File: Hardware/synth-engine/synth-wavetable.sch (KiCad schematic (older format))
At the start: 0 parts

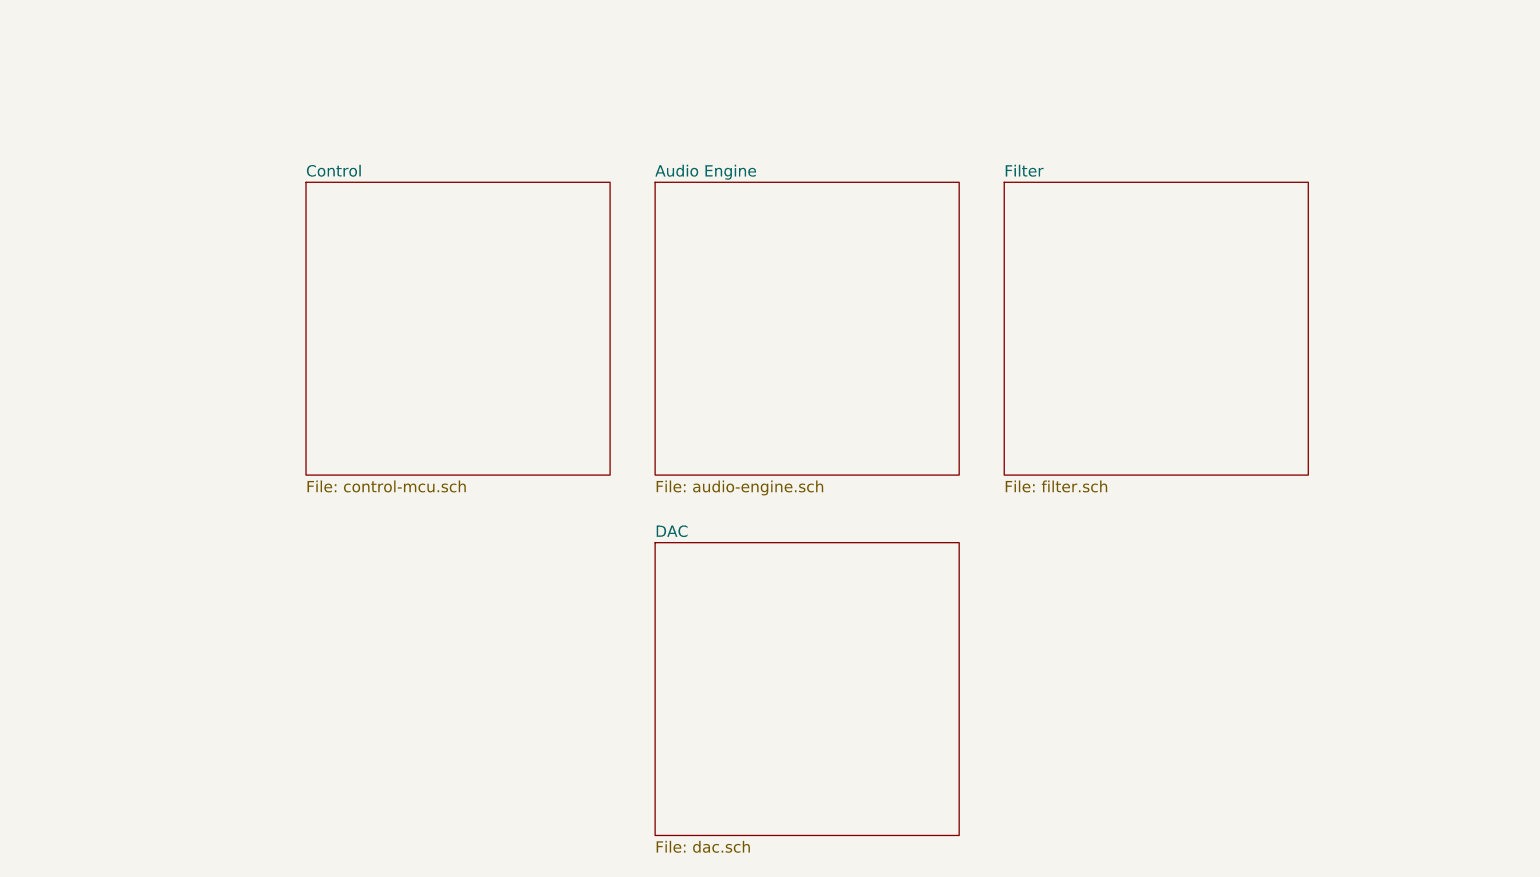
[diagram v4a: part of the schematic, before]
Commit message: add I/O connections between DAC and STM32 pages
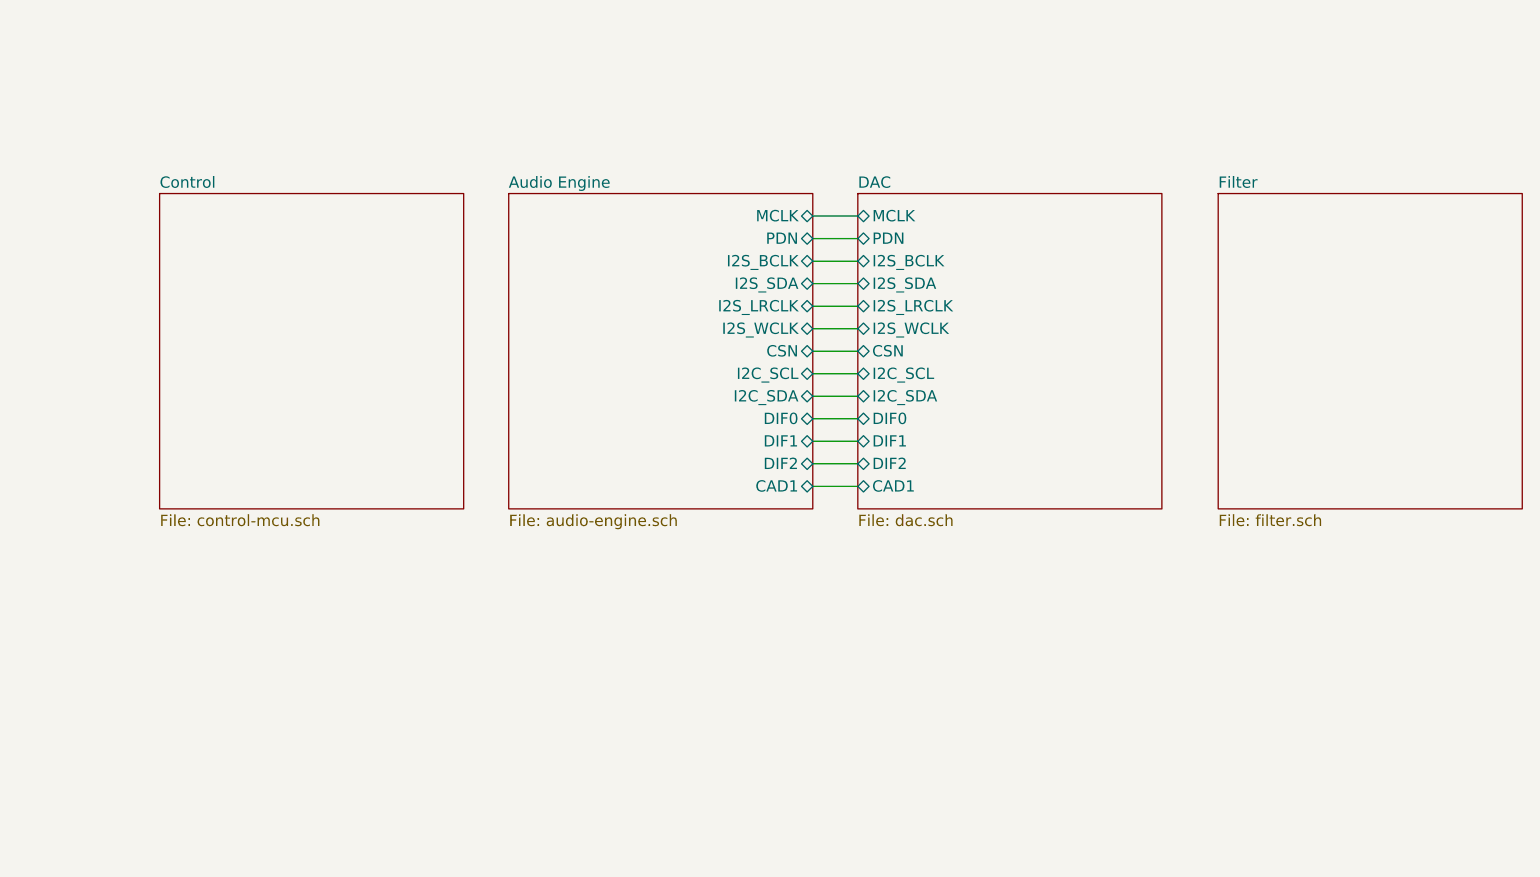
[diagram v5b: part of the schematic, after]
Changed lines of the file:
@@
 $EndDescr
 $Sheet
-S 3500 3450 1350 1300
+S 2850 3500 1350 1400
 U 5DDBDEEA
 F0 "Control" 50
@@
 $EndSheet
 $Sheet
-S 5050 3450 1350 1300
+S 4400 3500 1350 1400
 U 5DDC7BB6
 F0 "Audio Engine" 50
 F1 "audio-engine.sch" 50
+F2 "PDN" B R 5750 3700 50
+F3 "I2S_BCLK" B R 5750 3800 50
+F4 "I2S_SDA" B R 5750 3900 50
+F5 "I2S_LRCLK" B R 5750 4000 50
+F6 "I2S_WCLK" B R 5750 4100 50
+F7 "CSN" B R 5750 4200 50
+F8 "I2C_SCL" B R 5750 4300 50
+F9 "I2C_SDA" B R 5750 4400 50
+F10 "DIF0" B R 5750 4500 50
+F11 "DIF1" B R 5750 4600 50
+F12 "DIF2" B R 5750 4700 50
+F13 "MCLK" B R 5750 3600 50
+F14 "CAD1" B R 5750 4800 50
 $EndSheet
 $Sheet
-S 6600 3450 1350 1300
+S 7550 3500 1350 1400
 U 5DDC7E61
 F0 "Filter" 50
@@
 $EndSheet
 $Sheet
-S 5050 5050 1350 1300
+S 5950 3500 1350 1400
 U 5DD9C8DD
 F0 "DAC" 50
 F1 "dac.sch" 50
+F2 "MCLK" B L 5950 3600 50
+F3 "PDN" B L 5950 3700 50
+F4 "I2S_BCLK" B L 5950 3800 50
+F5 "I2S_SDA" B L 5950 3900 50
+F6 "I2S_LRCLK" B L 5950 4000 50
+F7 "I2S_WCLK" B L 5950 4100 50
+F8 "CSN" B L 5950 4200 50
+F9 "I2C_SCL" B L 5950 4300 50
+F10 "I2C_SDA" B L 5950 4400 50
+F11 "DIF0" B L 5950 4500 50
+F12 "DIF1" B L 5950 4600 50
+F13 "DIF2" B L 5950 4700 50
+F14 "CAD1" B L 5950 4800 50
 $EndSheet
+Wire Wire Line
+	5750 3600 5950 3600
+Wire Wire Line
+	5950 3700 5750 3700
+Wire Wire Line
+	5750 3800 5950 3800
+Wire Wire Line
+	5950 3900 5750 3900
+Wire Wire Line
+	5750 4000 5950 4000
+Wire Wire Line
+	5950 4100 5750 4100
+Wire Wire Line
+	5750 4200 5950 4200
+Wire Wire Line
+	5950 4300 5750 4300
+Wire Wire Line
+	5750 4400 5950 4400
+Wire Wire Line
+	5950 4500 5750 4500
+Wire Wire Line
+	5750 4600 5950 4600
+Wire Wire Line
+	5950 4700 5750 4700
+Wire Wire Line
+	5750 4800 5950 4800
 $EndSCHEMATC

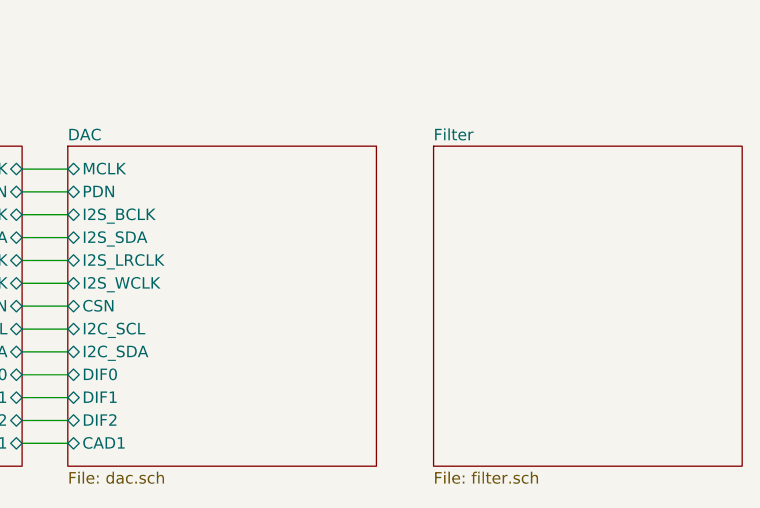
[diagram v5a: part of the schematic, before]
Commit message: add LFP following DAC diff outputs and connect DAC output to VCF input
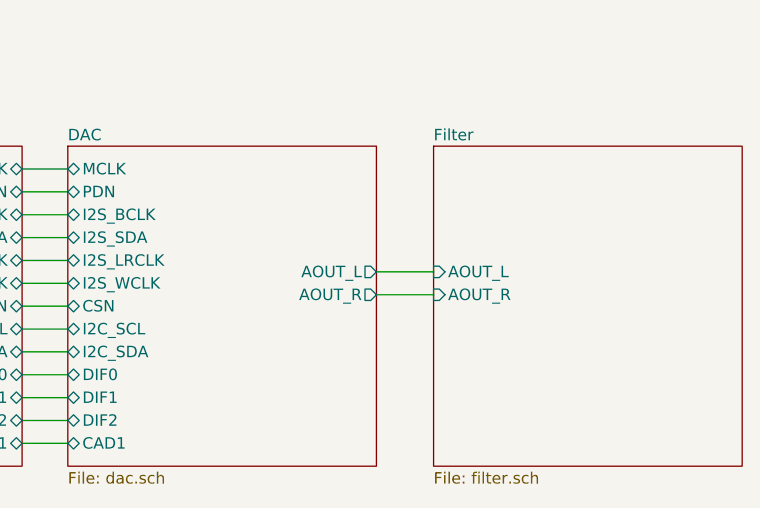
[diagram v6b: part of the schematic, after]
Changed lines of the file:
@@
 F0 "Filter" 50
 F1 "filter.sch" 50
+F2 "AOUT_L" I L 7550 4050 50
+F3 "AOUT_R" I L 7550 4150 50
 $EndSheet
 $Sheet
@@
 F13 "DIF2" B L 5950 4700 50
 F14 "CAD1" B L 5950 4800 50
+F15 "AOUT_L" O R 7300 4050 50
+F16 "AOUT_R" O R 7300 4150 50
 $EndSheet
 Wire Wire Line
@@
 Wire Wire Line
 	5750 4800 5950 4800
+Wire Wire Line
+	7300 4050 7550 4050
+Wire Wire Line
+	7300 4150 7550 4150
 $EndSCHEMATC

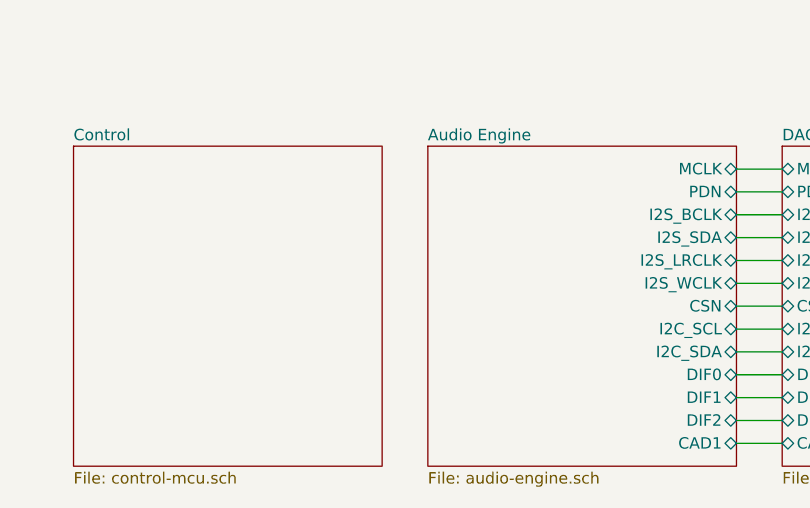
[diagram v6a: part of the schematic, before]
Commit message: assign footprints to schematic symbols.
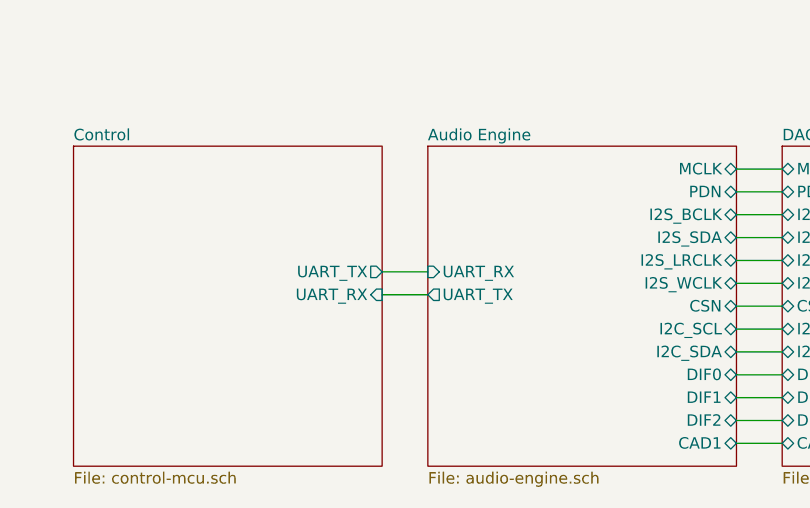
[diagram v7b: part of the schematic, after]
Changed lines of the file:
@@
 F0 "Control" 50
 F1 "control-mcu.sch" 50
+F2 "UART_TX" O R 4200 4050 50
+F3 "UART_RX" I R 4200 4150 50
 $EndSheet
 $Sheet
@@
 F13 "MCLK" B R 5750 3600 50
 F14 "CAD1" B R 5750 4800 50
+F15 "UART_TX" O L 4400 4150 50
+F16 "UART_RX" I L 4400 4050 50
 $EndSheet
 $Sheet
@@
 Wire Wire Line
 	7300 4150 7550 4150
+Wire Wire Line
+	4200 4150 4400 4150
+Wire Wire Line
+	4400 4050 4200 4050
 $EndSCHEMATC

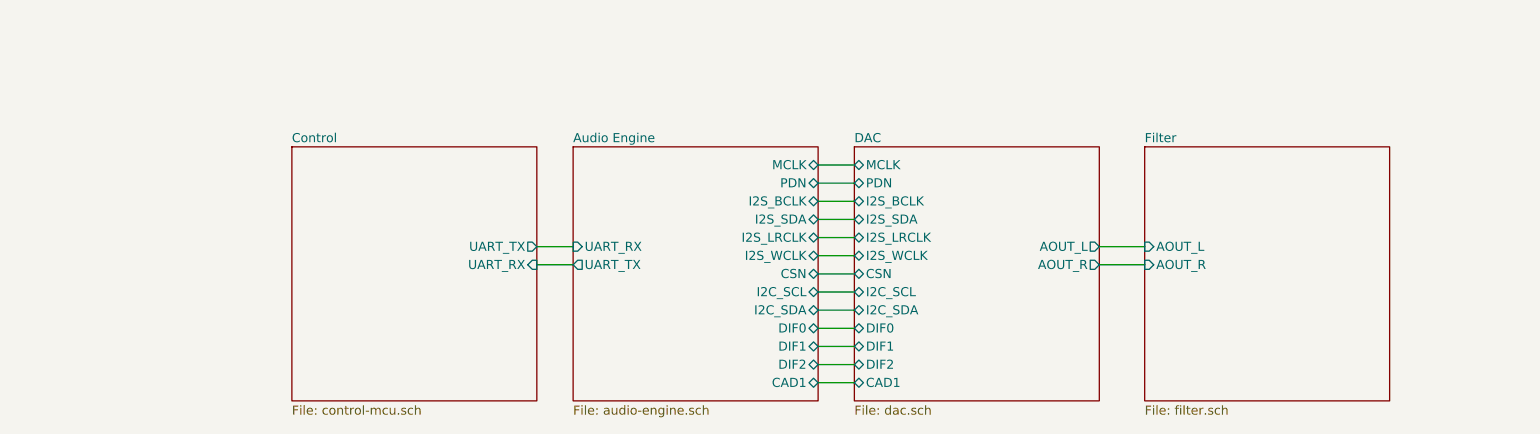
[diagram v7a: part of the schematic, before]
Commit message: add separate PCB with potentiometers and switches and connector between control board and synth engine
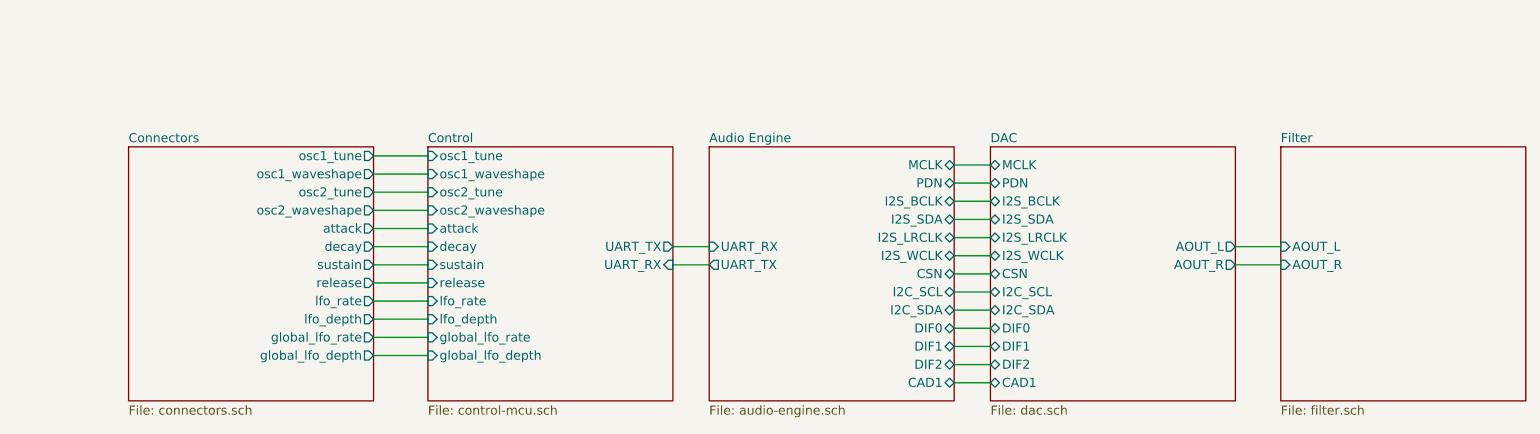
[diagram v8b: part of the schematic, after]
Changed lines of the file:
@@
 $Descr A4 11693 8268
 encoding utf-8
-Sheet 1 6
+Sheet 1 7
 Title ""
 Date ""
@@
 $EndDescr
 $Sheet
-S 2850 3500 1350 1400
+S 3600 3500 1350 1400
 U 5DDBDEEA
 F0 "Control" 50
 F1 "control-mcu.sch" 50
-F2 "UART_TX" O R 4200 4050 50
-F3 "UART_RX" I R 4200 4150 50
+F2 "UART_TX" O R 4950 4050 50
+F3 "UART_RX" I R 4950 4150 50
+F4 "osc1_tune" I L 3600 3550 50
+F5 "osc1_waveshape" I L 3600 3650 50
+F6 "osc2_tune" I L 3600 3750 50
+F7 "osc2_waveshape" I L 3600 3850 50
+F8 "attack" I L 3600 3950 50
+F9 "decay" I L 3600 4050 50
+F10 "sustain" I L 3600 4150 50
+F11 "release" I L 3600 4250 50
+F12 "lfo_rate" I L 3600 4350 50
+F13 "lfo_depth" I L 3600 4450 50
+F14 "global_lfo_rate" I L 3600 4550 50
+F15 "global_lfo_depth" I L 3600 4650 50
 $EndSheet
 $Sheet
-S 4400 3500 1350 1400
+S 5150 3500 1350 1400
 U 5DDC7BB6
 F0 "Audio Engine" 50
 F1 "audio-engine.sch" 50
-F2 "PDN" B R 5750 3700 50
-F3 "I2S_BCLK" B R 5750 3800 50
-F4 "I2S_SDA" B R 5750 3900 50
-F5 "I2S_LRCLK" B R 5750 4000 50
-F6 "I2S_WCLK" B R 5750 4100 50
-F7 "CSN" B R 5750 4200 50
-F8 "I2C_SCL" B R 5750 4300 50
-F9 "I2C_SDA" B R 5750 4400 50
-F10 "DIF0" B R 5750 4500 50
-F11 "DIF1" B R 5750 4600 50
-F12 "DIF2" B R 5750 4700 50
-F13 "MCLK" B R 5750 3600 50
-F14 "CAD1" B R 5750 4800 50
-F15 "UART_TX" O L 4400 4150 50
-F16 "UART_RX" I L 4400 4050 50
+F2 "PDN" B R 6500 3700 50
+F3 "I2S_BCLK" B R 6500 3800 50
+F4 "I2S_SDA" B R 6500 3900 50
+F5 "I2S_LRCLK" B R 6500 4000 50
+F6 "I2S_WCLK" B R 6500 4100 50
+F7 "CSN" B R 6500 4200 50
+F8 "I2C_SCL" B R 6500 4300 50
+F9 "I2C_SDA" B R 6500 4400 50
+F10 "DIF0" B R 6500 4500 50
+F11 "DIF1" B R 6500 4600 50
+F12 "DIF2" B R 6500 4700 50
+F13 "MCLK" B R 6500 3600 50
+F14 "CAD1" B R 6500 4800 50
+F15 "UART_TX" O L 5150 4150 50
+F16 "UART_RX" I L 5150 4050 50
 $EndSheet
 $Sheet
-S 7550 3500 1350 1400
+S 8300 3500 1350 1400
 U 5DDC7E61
 F0 "Filter" 50
 F1 "filter.sch" 50
-F2 "AOUT_L" I L 7550 4050 50
-F3 "AOUT_R" I L 7550 4150 50
+F2 "AOUT_L" I L 8300 4050 50
+F3 "AOUT_R" I L 8300 4150 50
 $EndSheet
 $Sheet
@@
 $EndSheet
 $Sheet
-S 5950 3500 1350 1400
+S 6700 3500 1350 1400
 U 5DD9C8DD
 F0 "DAC" 50
 F1 "dac.sch" 50
-F2 "MCLK" B L 5950 3600 50
-F3 "PDN" B L 5950 3700 50
-F4 "I2S_BCLK" B L 5950 3800 50
-F5 "I2S_SDA" B L 5950 3900 50
-F6 "I2S_LRCLK" B L 5950 4000 50
-F7 "I2S_WCLK" B L 5950 4100 50
-F8 "CSN" B L 5950 4200 50
-F9 "I2C_SCL" B L 5950 4300 50
-F10 "I2C_SDA" B L 5950 4400 50
-F11 "DIF0" B L 5950 4500 50
-F12 "DIF1" B L 5950 4600 50
-F13 "DIF2" B L 5950 4700 50
-F14 "CAD1" B L 5950 4800 50
-F15 "AOUT_L" O R 7300 4050 50
-F16 "AOUT_R" O R 7300 4150 50
+F2 "MCLK" B L 6700 3600 50
+F3 "PDN" B L 6700 3700 50
+F4 "I2S_BCLK" B L 6700 3800 50
+F5 "I2S_SDA" B L 6700 3900 50
+F6 "I2S_LRCLK" B L 6700 4000 50
+F7 "I2S_WCLK" B L 6700 4100 50
+F8 "CSN" B L 6700 4200 50
+F9 "I2C_SCL" B L 6700 4300 50
+F10 "I2C_SDA" B L 6700 4400 50
+F11 "DIF0" B L 6700 4500 50
+F12 "DIF1" B L 6700 4600 50
+F13 "DIF2" B L 6700 4700 50
+F14 "CAD1" B L 6700 4800 50
+F15 "AOUT_L" O R 8050 4050 50
+F16 "AOUT_R" O R 8050 4150 50
 $EndSheet
 Wire Wire Line
-	5750 3600 5950 3600
+	6500 3600 6700 3600
 Wire Wire Line
-	5950 3700 5750 3700
+	6700 3700 6500 3700
 Wire Wire Line
-	5750 3800 5950 3800
+	6500 3800 6700 3800
 Wire Wire Line
-	5950 3900 5750 3900
+	6700 3900 6500 3900
 Wire Wire Line
-	5750 4000 5950 4000
+	6500 4000 6700 4000
 Wire Wire Line
-	5950 4100 5750 4100
+	6700 4100 6500 4100
 Wire Wire Line
-	5750 4200 5950 4200
+	6500 4200 6700 4200
 Wire Wire Line
-	5950 4300 5750 4300
+	6700 4300 6500 4300
 Wire Wire Line
-	5750 4400 5950 4400
+	6500 4400 6700 4400
 Wire Wire Line
-	5950 4500 5750 4500
+	6700 4500 6500 4500
 Wire Wire Line
-	5750 4600 5950 4600
+	6500 4600 6700 4600
 Wire Wire Line
-	5950 4700 5750 4700
+	6700 4700 6500 4700
 Wire Wire Line
-	5750 4800 5950 4800
+	6500 4800 6700 4800
 Wire Wire Line
-	7300 4050 7550 4050
+	8050 4050 8300 4050
 Wire Wire Line
-	7300 4150 7550 4150
+	8050 4150 8300 4150
 Wire Wire Line
-	4200 4150 4400 4150
+	4950 4150 5150 4150
 Wire Wire Line
-	4400 4050 4200 4050
+	5150 4050 4950 4050
+$Sheet
+S 1950 3500 1350 1400
+U 5DDCA8E8
+F0 "Connectors" 50
+F1 "connectors.sch" 50
+F2 "osc1_tune" O R 3300 3550 50
+F3 "osc1_waveshape" O R 3300 3650 50
+F4 "osc2_tune" O R 3300 3750 50
+F5 "osc2_waveshape" O R 3300 3850 50
+F6 "attack" O R 3300 3950 50
+F7 "decay" O R 3300 4050 50
+F8 "sustain" O R 3300 4150 50
+F9 "release" O R 3300 4250 50
+F10 "lfo_rate" O R 3300 4350 50
+F11 "lfo_depth" O R 3300 4450 50
+F12 "global_lfo_rate" O R 3300 4550 50
+F13 "global_lfo_depth" O R 3300 4650 50
+$EndSheet
+Wire Wire Line
+	3300 3550 3600 3550
+Wire Wire Line
+	3300 3650 3600 3650
+Wire Wire Line
+	3300 3750 3600 3750
+Wire Wire Line
+	3300 3850 3600 3850
+Wire Wire Line
+	3300 3950 3600 3950
+Wire Wire Line
+	3300 4050 3600 4050
+Wire Wire Line
+	3300 4150 3600 4150
+Wire Wire Line
+	3300 4250 3600 4250
+Wire Wire Line
+	3300 4350 3600 4350
+Wire Wire Line
+	3300 4450 3600 4450
+Wire Wire Line
+	3300 4550 3600 4550
+Wire Wire Line
+	3300 4650 3600 4650
 $EndSCHEMATC
